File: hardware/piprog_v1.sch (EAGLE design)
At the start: 20 parts, among them U1 EEPROM-I2CSMD, X1 RASPI_BOARD_B+#_HD

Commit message: changed reset pin, add reset pullup
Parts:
- added R8: 10k, SparkFun-Passives:RESISTORPTH-1/4W
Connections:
- net RST: now also R8.1, X1.GPIO25; no longer X1.GPIO12
- net VCC: now also R8.2
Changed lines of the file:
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@@
 <part name="S1" library="SparkFun-Electromechanical" deviceset="SWITCH-MOMENTARY-2" device="PTH" value=""/>
 <part name="GND6" library="SparkFun-Aesthetics" deviceset="GND" device=""/>
+<part name="VCC1" library="SparkFun-Aesthetics" deviceset="3.3V" device=""/>
+<part name="R8" library="SparkFun-Passives" deviceset="RESISTOR" device="PTH-1/4W" value="10k"/>
 </parts>
 <sheets>
@@
 <instance part="S1" gate="G$1" x="-45.72" y="58.42" rot="R90"/>
 <instance part="GND6" gate="1" x="-45.72" y="30.48"/>
+<instance part="VCC1" gate="G$1" x="-30.48" y="132.08"/>
+<instance part="R8" gate="G$1" x="-30.48" y="101.6" rot="R90"/>
 </instances>
 <busses>
@@
 <junction x="-2.54" y="38.1"/>
 </segment>
+<segment>
+<pinref part="R8" gate="G$1" pin="2"/>
+<pinref part="VCC1" gate="G$1" pin="3.3V"/>
+<wire x1="-30.48" y1="106.68" x2="-30.48" y2="132.08" width="0.1524" layer="91"/>
+</segment>
 </net>
 <net name="SCK" class="0">
@@
 </segment>
 <segment>
-<pinref part="X1" gate="G$1" pin="GPIO12"/>
-<wire x1="-17.78" y1="81.28" x2="-27.94" y2="81.28" width="0.1524" layer="91"/>
-<label x="-27.94" y="81.28" size="1.778" layer="95"/>
+<pinref part="X1" gate="G$1" pin="GPIO25"/>
+<wire x1="-17.78" y1="93.98" x2="-30.48" y2="93.98" width="0.1524" layer="91"/>
+<label x="-25.4" y="93.98" size="1.778" layer="95"/>
+<pinref part="R8" gate="G$1" pin="1"/>
+<wire x1="-30.48" y1="93.98" x2="-30.48" y2="96.52" width="0.1524" layer="91"/>
 </segment>
 </net>

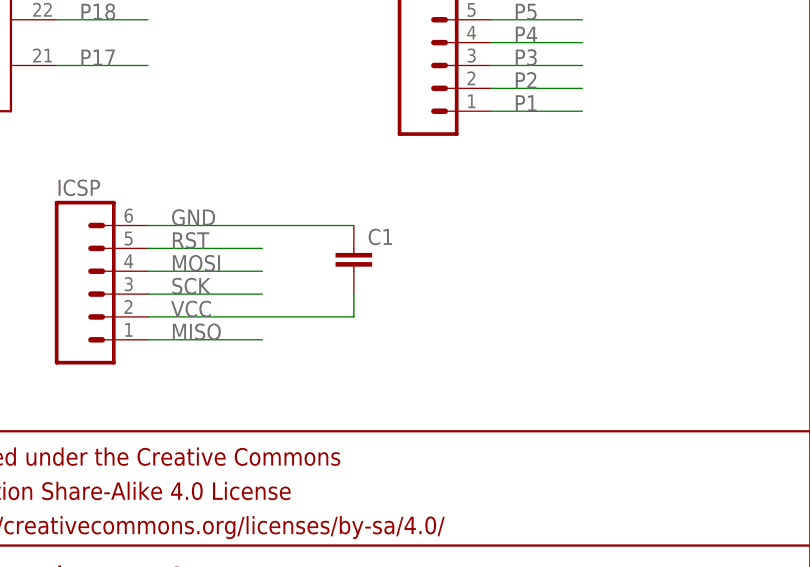
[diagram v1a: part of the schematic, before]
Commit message: changed reset pin, add reset pullup
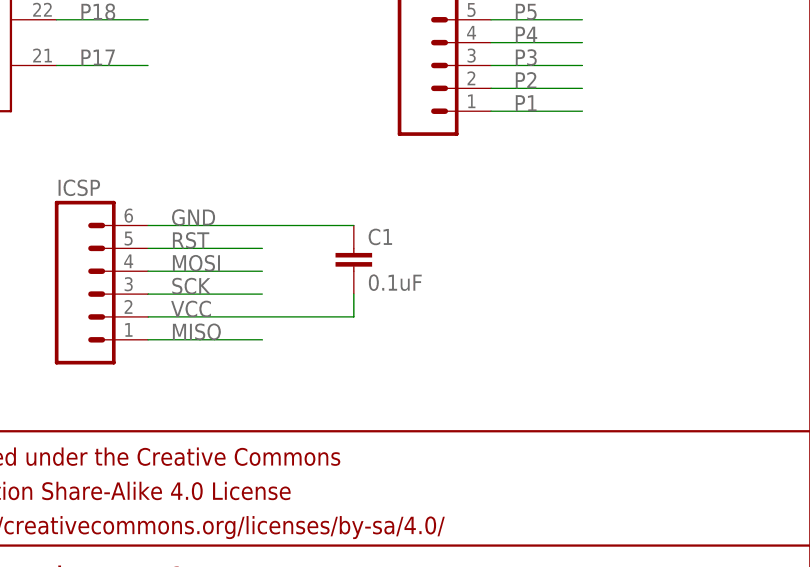
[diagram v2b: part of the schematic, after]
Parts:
- C1: value (none) -> 0.1uF
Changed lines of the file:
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@@
 <part name="GND5" library="SparkFun-Aesthetics" deviceset="GND" device=""/>
 <part name="FRAME1" library="SparkFun-Aesthetics" deviceset="FRAME-LETTER" device="NO_PACKAGE"/>
-<part name="C1" library="SparkFun-Passives" deviceset="CAP" device="PTH"/>
+<part name="C1" library="SparkFun-Passives" deviceset="CAP" device="PTH" value="0.1uF"/>
 <part name="R1" library="SparkFun-Passives" deviceset="RESISTOR" device="PTH-1/4W" value="3.9k"/>
 <part name="R2" library="SparkFun-Passives" deviceset="RESISTOR" device="PTH-1/4W" value="3.9k"/>
